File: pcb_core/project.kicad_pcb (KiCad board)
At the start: 2 copper layers, 18.3 x 20.8 mm, 38 parts, among them IC1 TCA9548APWR

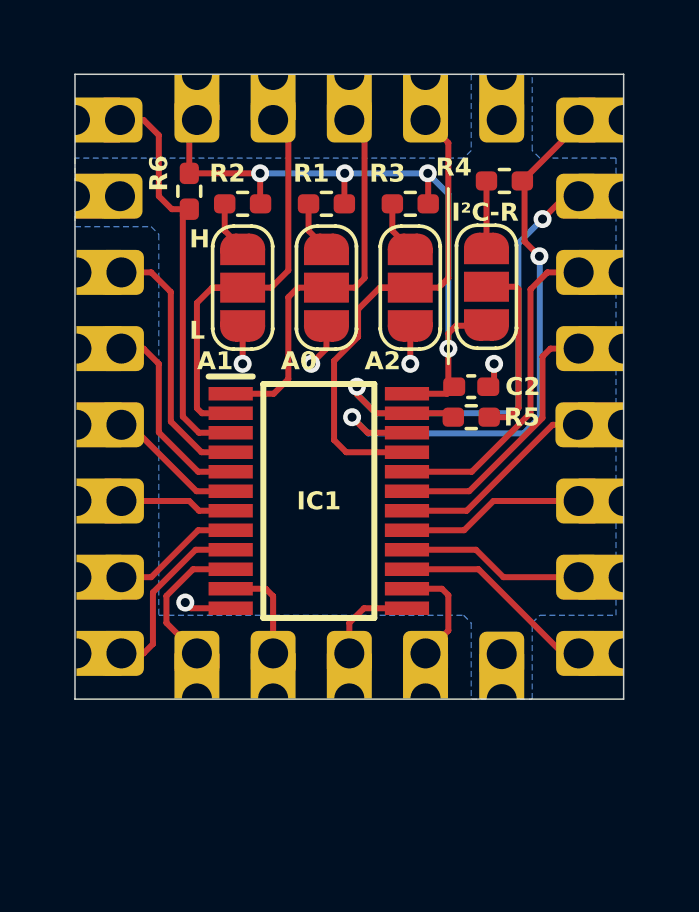
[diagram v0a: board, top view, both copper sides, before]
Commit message: Remove connector on own side
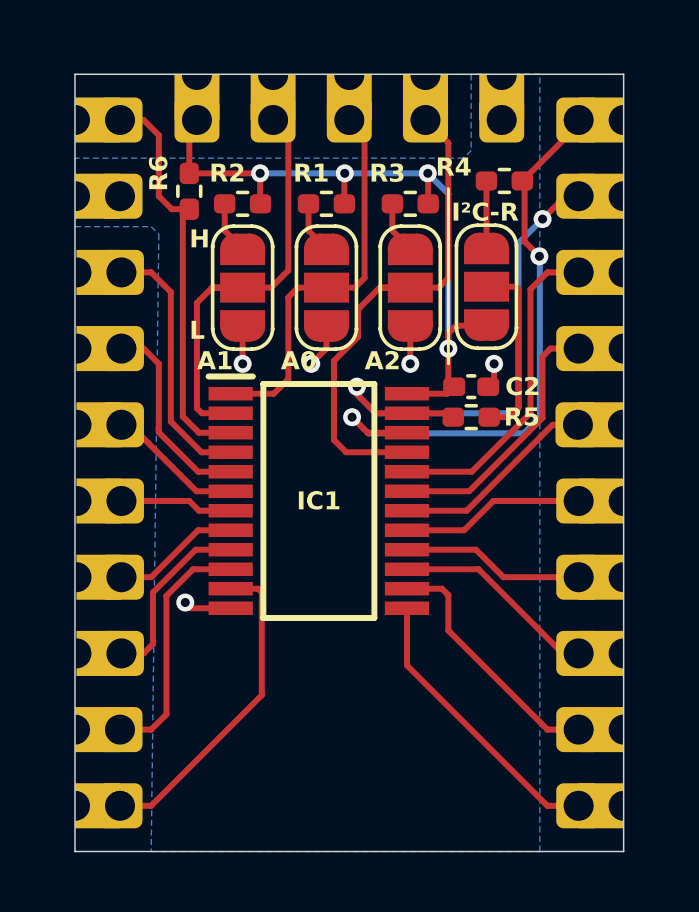
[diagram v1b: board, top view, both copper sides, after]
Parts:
- removed J25: ~, Castellated_Holes:Castellated_Hole02
- added QR*****: https://github.com/fanningert/kicad_pcb_i2cmultiplexer, https://github.com/fanningert/kicad_pcb_i2cmultiplexer, B.Cu at (133.9, 72.1)
- moved J19 9.82 mm to (143.0, 77.5), turned to 180 degrees
- moved J12 7.51 mm to (124.7, 77.5), turned to 0 degrees
- moved J20 6.69 mm to (143.0, 74.9), turned to 180 degrees
- moved J11 4.19 mm to (124.7, 74.9), turned to 0 degrees
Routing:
- net /SC3: track 3.42 -> 10.8 mm
- net /SD4: track 3.14 -> 9.56 mm
- net /SC4: track 4.24 -> 8.36 mm
- net /SD3: track 5.10 -> 8.22 mm
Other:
- board size 18.3 x 20.8 mm -> 18.3 x 25.9 mm
